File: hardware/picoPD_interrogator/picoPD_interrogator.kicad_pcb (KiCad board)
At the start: 4 copper layers, 81.9 x 18.8 mm, 94 parts, among them J4 Extra Pins, J5 Conn_01x04, J6 SM03B-SRSS-TB, J7 SM04B-SRSS-TB, Q1 rohm-RE1C002UN, Q2 rohm-RE1C002UN, Q3 rohm-RE1C002UN, Q4 rohm-RE1C002UN, Q5 rohm-RE1C002UN, Q6 rohm-RE1C002UN, SW1 SW_Push, SW2 SW_Push, U1 RP2350_60QFN, U10 W25Q128JVS, U2 ST-LM393QT, U7 LV2862XDDC, Y1 Crystal_GND24

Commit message: PCB: Getting PCB ready for Gerber generation.
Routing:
- net /3V3: track 104.1 -> 105.8 mm
- net /P1_VBUS: track 19.7 -> 20.7 mm
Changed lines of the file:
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@@
 		(fp_arc
 			(start 3.521125 1.286294)
-			(mid 3.477135 1.233898)
+			(mid 3.477135 1.233899)
 			(end 3.435 1.18)
 			(stroke
@@
 		(fp_arc
 			(start 3.93363 -1.644317)
-			(mid 4.00637 -1.689264)
+			(mid 4.006369 -1.689267)
 			(end 4.081 -1.731)
 			(stroke
@@
 		(fp_arc
 			(start 5.000479 1.960685)
-			(mid 4.744554 1.943974)
+			(mid 4.744554 1.943973)
 			(end 4.493 1.894)
 			(stroke
@@
 		(fp_arc
 			(start 5.638712 -1.85392)
-			(mid 5.734863 -1.817952)
+			(mid 5.734863 -1.817951)
 			(end 5.829 -1.777)
 			(stroke
@@
 		(fp_arc
 			(start 5.829295 1.77705)
-			(mid 5.735154 1.818015)
+			(mid 5.735155 1.818016)
 			(end 5.639 1.854)
 			(stroke
@@
 		(fp_arc
 			(start 5.920652 -1.730826)
-			(mid 5.995275 -1.689024)
+			(mid 5.995274 -1.689022)
 			(end 6.068 -1.644)
 			(stroke
@@
 		(fp_arc
 			(start 6.096479 -1.625751)
-			(mid 6.166349 -1.576375)
+			(mid 6.166348 -1.576374)
 			(end 6.234 -1.524)
 			(stroke
@@
 		(fp_arc
 			(start 6.233457 1.523294)
-			(mid 6.165839 1.575648)
+			(mid 6.16584 1.575649)
 			(end 6.096 1.625)
 			(stroke
@@
 		(fp_arc
 			(start 8.521125 1.286294)
-			(mid 8.477135 1.233898)
+			(mid 8.477135 1.233899)
 			(end 8.435 1.18)
 			(stroke
@@
 		(fp_arc
 			(start 8.93363 -1.644317)
-			(mid 9.00637 -1.689264)
+			(mid 9.006369 -1.689267)
 			(end 9.081 -1.731)
 			(stroke
@@
 		(fp_arc
 			(start 10.000479 1.960685)
-			(mid 9.744554 1.943974)
+			(mid 9.744554 1.943973)
 			(end 9.493 1.894)
 			(stroke
@@
 		(fp_arc
 			(start 10.638712 -1.85392)
-			(mid 10.734863 -1.817952)
+			(mid 10.734863 -1.817951)
 			(end 10.829 -1.777)
 			(stroke
@@
 		(fp_arc
 			(start 10.829295 1.77705)
-			(mid 10.735154 1.818015)
+			(mid 10.735155 1.818016)
 			(end 10.639 1.854)
 			(stroke
@@
 		(fp_arc
 			(start 10.920652 -1.730826)
-			(mid 10.995275 -1.689024)
+			(mid 10.995274 -1.689022)
 			(end 11.068 -1.644)
 			(stroke
@@
 		(fp_arc
 			(start 11.096479 -1.625751)
-			(mid 11.166349 -1.576375)
+			(mid 11.166348 -1.576374)
 			(end 11.234 -1.524)
 			(stroke
@@
 		(fp_arc
 			(start 11.233457 1.523294)
-			(mid 11.165839 1.575648)
+			(mid 11.16584 1.575649)
 			(end 11.096 1.625)
 			(stroke
@@
 		(fp_arc
 			(start 13.521125 1.286294)
-			(mid 13.477135 1.233898)
+			(mid 13.477135 1.233899)
 			(end 13.435 1.18)
 			(stroke
@@
 		(fp_arc
 			(start 13.93363 -1.644317)
-			(mid 14.00637 -1.689264)
+			(mid 14.006369 -1.689267)
 			(end 14.081 -1.731)
 			(stroke
@@
 		(fp_arc
 			(start 15.000479 1.960685)
-			(mid 14.744554 1.943974)
+			(mid 14.744554 1.943973)
 			(end 14.493 1.894)
 			(stroke
@@
 		(fp_arc
 			(start 15.638712 -1.85392)
-			(mid 15.734863 -1.817952)
+			(mid 15.734863 -1.817951)
 			(end 15.829 -1.777)
 			(stroke
@@
 		(fp_arc
 			(start 15.829295 1.77705)
-			(mid 15.735154 1.818015)
+			(mid 15.735155 1.818016)
 			(end 15.639 1.854)
 			(stroke
@@
 		(fp_arc
 			(start 15.920652 -1.730826)
-			(mid 15.995275 -1.689024)
+			(mid 15.995274 -1.689022)
 			(end 16.068 -1.644)
 			(stroke
@@
 		(fp_arc
 			(start 16.096479 -1.625751)
-			(mid 16.166349 -1.576375)
+			(mid 16.166348 -1.576374)
 			(end 16.234 -1.524)
 			(stroke
@@
 		(fp_arc
 			(start 16.233457 1.523294)
-			(mid 16.165839 1.575648)
+			(mid 16.16584 1.575649)
 			(end 16.096 1.625)
 			(stroke
@@
 		(at 135.63 101.32 -90)
 		(property "Reference" "U4"
-			(at 0 -2.75 270)
+			(at 0 -2.75 -90)
 			(unlocked yes)
 			(layer "F.SilkS")
@@
 		(at 144.3 94.7 -90)
 		(property "Reference" "U8"
-			(at -0.62 -2.54 270)
+			(at -0.62 -2.54 -90)
 			(unlocked yes)
 			(layer "F.SilkS")
@@
 		(tags "capacitor")
 		(property "Reference" "C15"
-			(at 0 -1.05 270)
+			(at 0 -1.05 -90)
 			(layer "F.SilkS")
 			(hide yes)
@@
 	)
 	(segment
+		(start 189.675 101.125)
+		(end 190.155 101.125)
+		(width 0.2)
+		(layer "F.Cu")
+		(net 25)
+	)
+	(segment
 		(start 179.03 100.47)
 		(end 179.77 99.73)
@@
 		(net 25)
 	)
+	(segment
+		(start 190.155 101.125)
+		(end 190.53 101.5)
+		(width 0.2)
+		(layer "F.Cu")
+		(net 25)
+	)
 	(via
 		(at 190.46 98.64)
@@
 	)
 	(segment
+		(start 129.83 105.175)
+		(end 129.85 105.195)
+		(width 0.2)
+		(layer "F.Cu")
+		(net 31)
+	)
+	(segment
 		(start 159.3125 101.2)
 		(end 158.84935 101.2)
@@
 	)
 	(segment
-		(start 129.955 105.3)
-		(end 130.625 105.3)
-		(width 0.2)
-		(layer "F.Cu")
-		(net 31)
-	)
-	(segment
-		(start 129.85 105.195)
-		(end 129.17 105.195)
-		(width 0.2)
-		(layer "F.Cu")
-		(net 31)
-	)
-	(segment
 		(start 161.675 101.794974)
 		(end 161.675 103.58)
@@
 	)
 	(segment
+		(start 129.955 105.3)
+		(end 129.85 105.195)
+		(width 0.2)
+		(layer "F.Cu")
+		(net 31)
+	)
+	(segment
 		(start 177.86 103.32)
 		(end 177.86 102.545001)
@@
 	)
 	(segment
-		(start 129.85 105.195)
+		(start 130.625 105.3)
 		(end 129.955 105.3)
 		(width 0.2)
@@
 	)
 	(segment
+		(start 129.15 105.175)
+		(end 129.83 105.175)
+		(width 0.2)
+		(layer "F.Cu")
+		(net 31)
+	)
+	(segment
 		(start 157.075 102.97435)
 		(end 157.075 103.4375)
@@
 	)
 	(segment
+		(start 156.07 105.94)
+		(end 156.15 106.02)
+		(width 0.2)
+		(layer "In2.Cu")
+		(net 31)
+	)
+	(segment
+		(start 157.1 107.075)
+		(end 157.1 106.97)
+		(width 0.2)
+		(layer "In2.Cu")
+		(net 31)
+	)
+	(segment
+		(start 157.1 106.97)
+		(end 156.07 105.94)
+		(width 0.2)
+		(layer "In2.Cu")
+		(net 31)
+	)
+	(segment
 		(start 169.560661 98.335)
 		(end 170.2 98.335)
@@
 	)
 	(segment
+		(start 191.325 100.875)
+		(end 190.675 100.875)
+		(width 0.2)
+		(layer "F.Cu")
+		(net 55)
+	)
+	(segment
 		(start 190.705 100.875)
 		(end 190.65 100.93)
@@
 	)
 	(segment
-		(start 166.475 94.175)
-		(end 167 94.7)
+		(start 190.675 100.875)
+		(end 190.65 100.9)
 		(width 0.2)
 		(layer "F.Cu")
@@
 	)
 	(segment
-		(start 191.325 100.875)
-		(end 190.705 100.875)
+		(start 166.475 94.175)
+		(end 167 94.7)
 		(width 0.2)
 		(layer "F.Cu")
@@
 	)
 	(via
-		(at 190.65 100.93)
+		(at 190.65 100.9)
 		(size 0.4)
 		(drill 0.3)
@@
 	)
 	(segment
+		(start 190.625 100.875)
+		(end 190.65 100.9)
+		(width 0.2)
+		(layer "In1.Cu")
+		(net 55)
+	)
+	(segment
 		(start 188.158513 94.123461)
 		(end 188.158513 98.575)
@@
 	(segment
 		(start 188.55 100.875)
-		(end 190.595 100.875)
+		(end 190.625 100.875)
 		(width 0.2)
 		(layer "In1.Cu")
@@
 			(pts
 				(xy 127.465 98.05) (xy 130.69 98.05) (xy 130.715 102.1) (xy 132.12 106.38) (xy 155.7 106.71) (xy 156.01 107.46)
-				(xy 157.95 107.46) (xy 158.33 106.74) (xy 168.53 106.75) (xy 168.56 93.5) (xy 172.52 93.52) (xy 172.49 108.92)
+				(xy 157.95 107.46) (xy 158.33 106.74) (xy 168.79 106.75) (xy 168.78 93.65) (xy 172.52 93.52) (xy 172.49 108.92)
 				(xy 129.79 108.88) (xy 128.81 104.84) (xy 127.325 101.7)
 			)

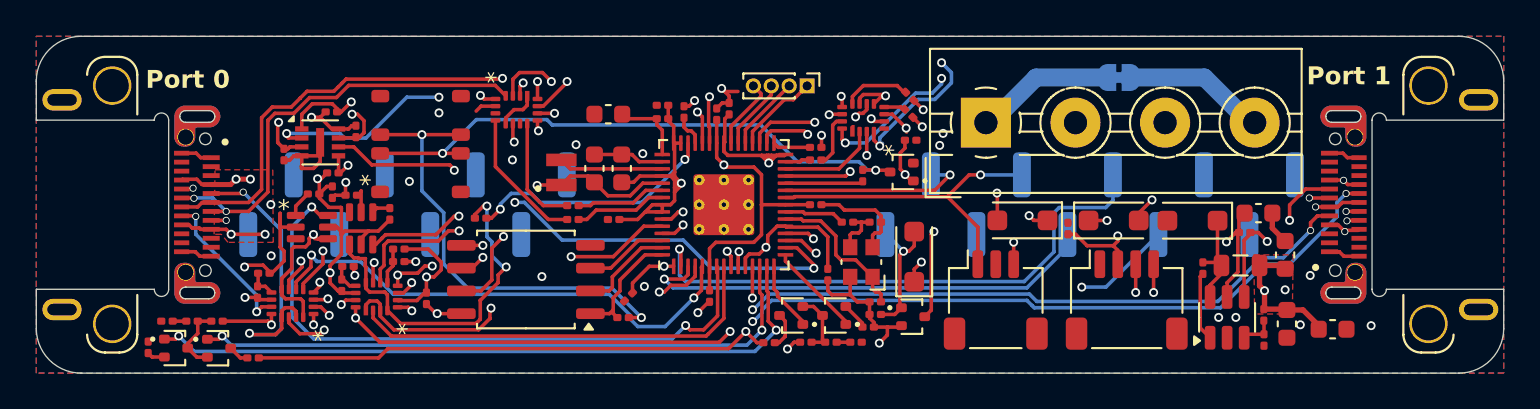
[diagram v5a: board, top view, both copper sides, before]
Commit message: Fixing spacing issues for PCBWay manufacturing.
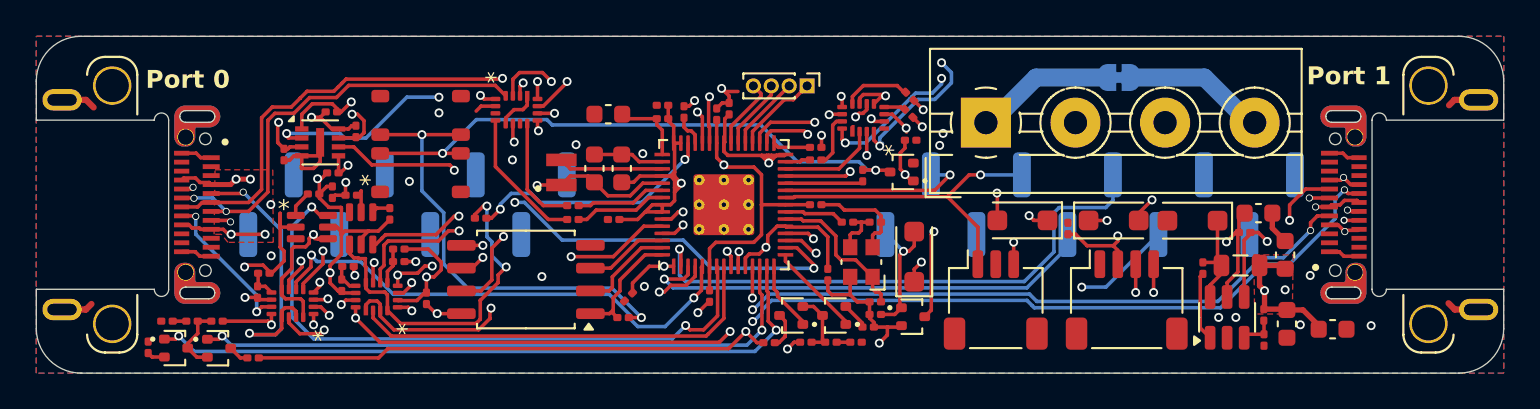
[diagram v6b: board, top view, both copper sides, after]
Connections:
- J1 pad SH: (no net) -> GND
- J3 pad SH: (no net) -> GND
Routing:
- net GND: track 59.5 -> 66.8 mm
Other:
- board text added: "Concerning the USB-C ports: The mounting holes inside the dotted lines should be plated through-holes. I've marked non-plated mounting holes with an X."

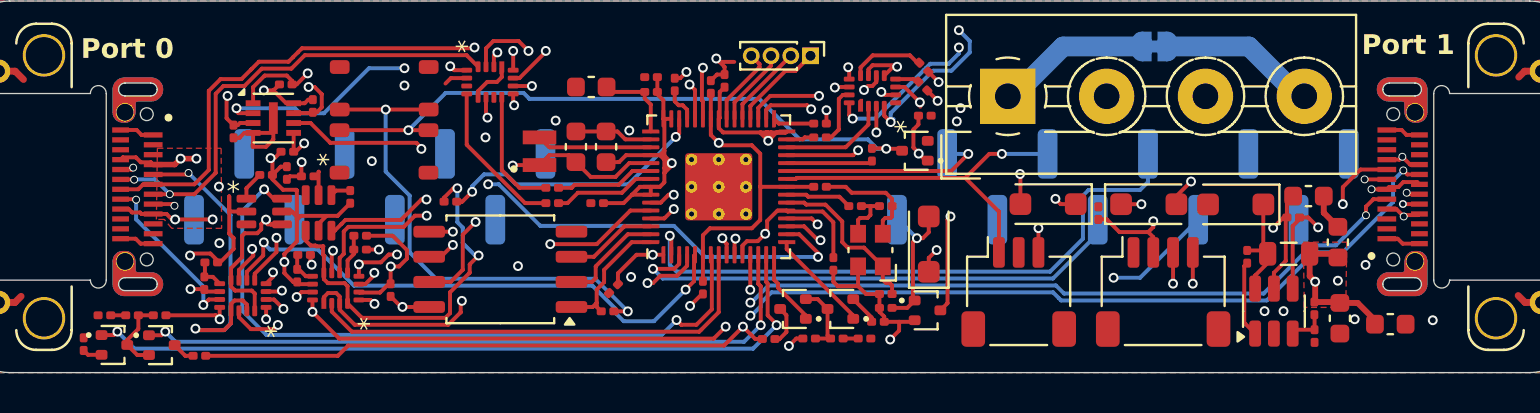
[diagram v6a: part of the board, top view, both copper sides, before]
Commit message: PCB: Reworked for the second try with PCBWAY.
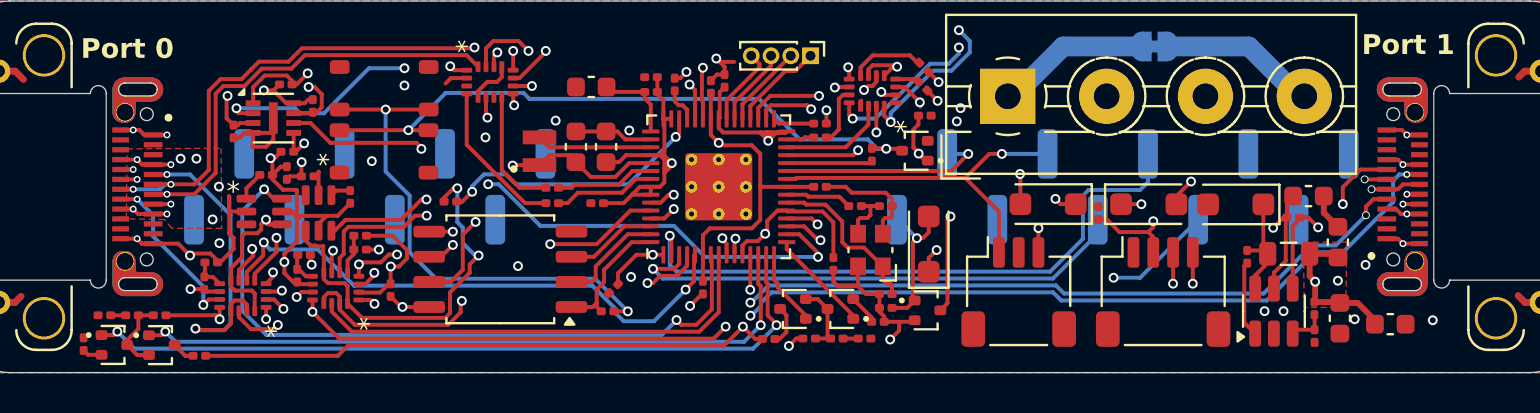
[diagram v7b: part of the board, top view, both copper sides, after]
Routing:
- net /P0_VBUS: track 26.4 -> 22.5 mm, vias 5 -> 8
- net GND: track 66.8 -> 69.7 mm, vias 18 -> 23
- net /USB_PD/P0_SBU2: track 52.6 -> 50.7 mm
- net /USB_PD/P0_DP: track 26.4 -> 27.3 mm, vias 2 -> 4
